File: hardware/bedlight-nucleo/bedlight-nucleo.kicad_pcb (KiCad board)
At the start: 2 copper layers, 76 x 76 mm, 10 parts, among them SW1 SW_Push, SW2 SW_Push, SW3 SW_Push, SW4 SW_Push, U1 Nucleo-32, U2 ULN2003A

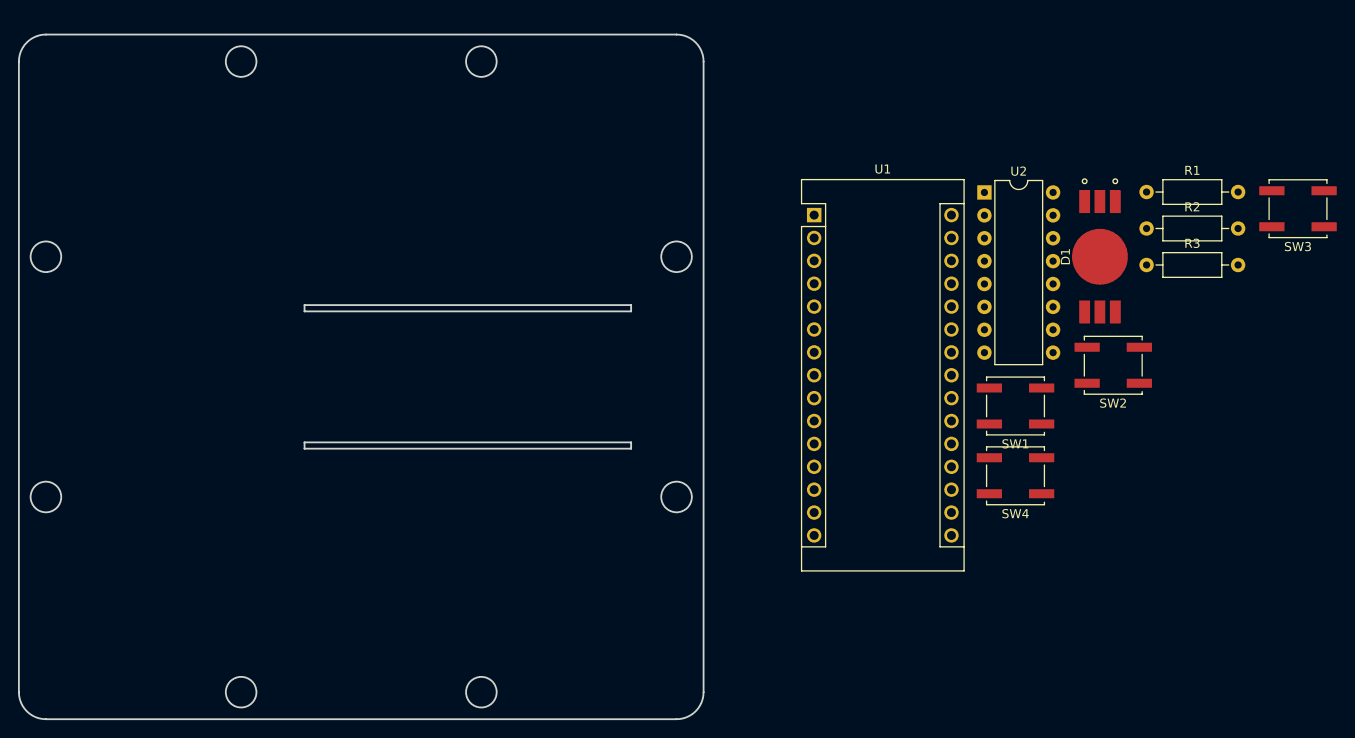
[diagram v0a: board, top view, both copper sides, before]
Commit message: Footprints partially placed
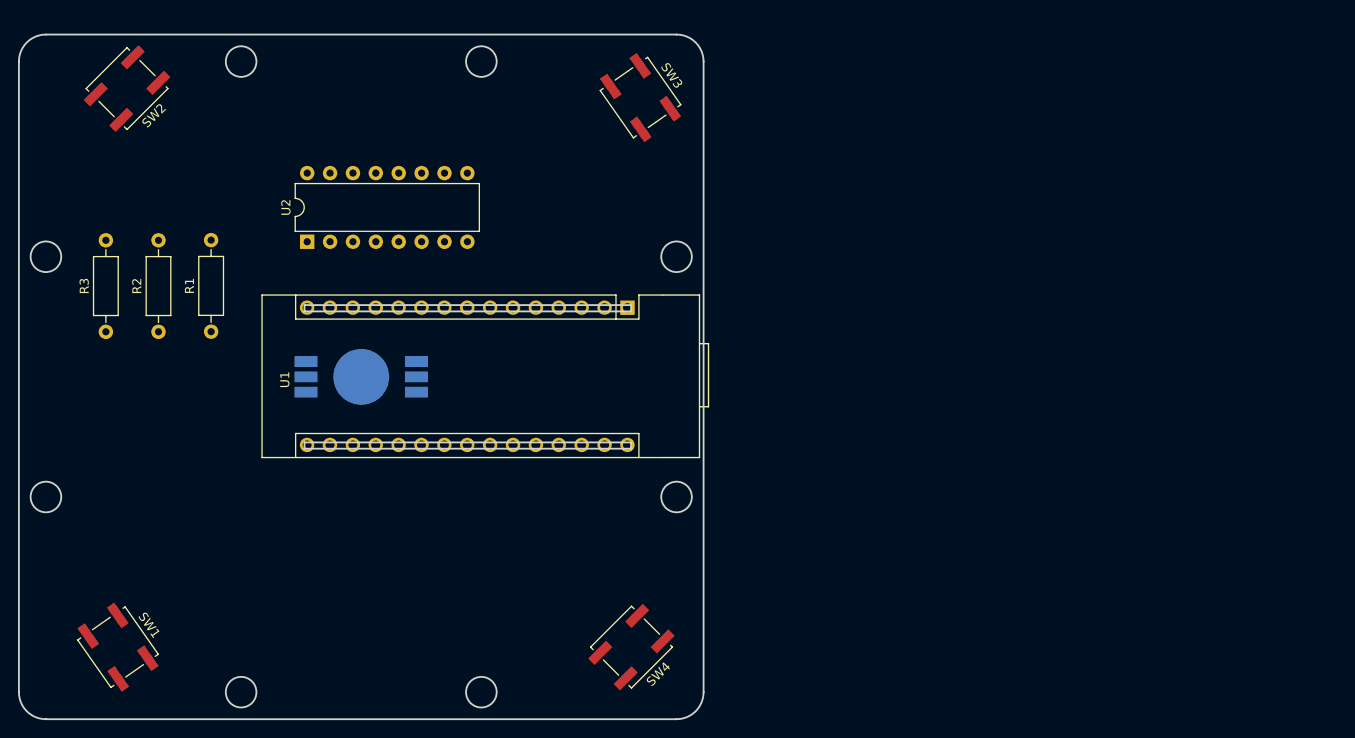
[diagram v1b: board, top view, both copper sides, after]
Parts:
- D1: moved to B.Cu
- U1: footprint Module:Arduino_Nano -> bedlight-nucleo:Nucleo-32
- moved R3 115.8 mm to (135.7, 107.3), turned to 90 degrees
- moved SW2 113.7 mm to (138.0, 80.3), turned to 45 degrees
- moved R2 110.3 mm to (141.5, 107.3), turned to 90 degrees
- moved R1 105.0 mm to (147.3, 107.3), turned to 90 degrees
- moved SW1 103.2 mm to (137.0, 142.3), turned to 125 degrees
- moved D1 83.1 mm to (164.0, 112.3), turned to 90 degrees
- moved U2 75.4 mm to (158.0, 97.3), turned to 90 degrees
- moved SW3 74.0 mm to (195.0, 81.3), turned to 125 degrees
- moved SW4 46.7 mm to (194.0, 142.3), turned to 45 degrees
- moved U1 23.1 mm to (193.5, 104.6), turned to 270 degrees
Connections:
- U1 pad 10: Net-(U1-Pad10) -> /OUT3
- U1 pad 11: Net-(U1-Pad11) -> /OUT2
- U1 pad 12: Net-(U1-Pad12) -> /OUT1
- U1 pad 13: Net-(U1-Pad13) -> /LED_RED
- U1 pad 14: /LED_RED -> /LED_GREEN
- U1 pad 15: /LED_GREEN -> /LED_BLUE
- U1 pad 16: /LED_BLUE -> Net-(U1-Pad16)
- U1 pad 9: Net-(U1-Pad9) -> /OUT4
- U2 pad 4: Net-(U2-Pad4) -> /OUT1
- U2 pad 5: Net-(U2-Pad5) -> /OUT2
- U2 pad 6: Net-(U2-Pad6) -> /OUT3
- U2 pad 7: Net-(U2-Pad7) -> /OUT4

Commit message: Routed
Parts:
- moved R3 10.9 mm to (146.5, 107.4)
- moved R1 10.2 mm to (137.1, 107.3)
- moved SW2 6.00 mm to (132.0, 80.3)
- moved SW1 5.39 mm to (132.0, 144.3), turned to 135 degrees
- moved SW4 2.83 mm to (196.0, 144.3)
- moved SW3 1.41 mm to (196.0, 80.3), turned to 135 degrees
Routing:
- net GND: track 0.00 -> 246.2 mm
- net /BUTTON2: track 0.00 -> 94.7 mm, vias 0 -> 1
- net /BUTTON1: track 0.00 -> 68.6 mm
- net +5V: track 0.00 -> 56.5 mm
- net /BUTTON3: track 0.00 -> 52.7 mm
- net /BUTTON4: track 0.00 -> 35.5 mm
- net Net-(R1-Pad2): track 0.00 -> 26.9 mm
- net Net-(D1-Pad1): track 0.00 -> 26.1 mm
- net Net-(R2-Pad2): track 0.00 -> 23.9 mm
- net Net-(R3-Pad2): track 0.00 -> 22.3 mm
- net Net-(D1-Pad2): track 0.00 -> 18.5 mm
- net Net-(D1-Pad3): track 0.00 -> 12.7 mm
- net /LED_BLUE: track 0.00 -> 7.42 mm
- net /OUT4: track 0.00 -> 7.32 mm
- net /OUT3: track 0.00 -> 7.32 mm
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- added copper zone on F.Cu, net GND
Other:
- outline, holes or cut-outs redrawn

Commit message: Added mounting holes
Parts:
- added H1: MountingHole, MountingHole:MountingHole_3.2mm_M3_DIN965_Pad, F.Cu at (177.3, 77.3)
- added H2: MountingHole, MountingHole:MountingHole_3.2mm_M3_DIN965_Pad, F.Cu at (129.0, 99.0)
- added H3: MountingHole, MountingHole:MountingHole_3.2mm_M3_DIN965_Pad, F.Cu at (150.7, 77.3)
- added H4: MountingHole, MountingHole:MountingHole_3.2mm_M3_DIN965_Pad, F.Cu at (129.0, 125.7)
- added H5: MountingHole, MountingHole:MountingHole_3.2mm_M3_DIN965_Pad, F.Cu at (199.0, 125.7)
- added H6: MountingHole, MountingHole:MountingHole_3.2mm_M3_DIN965_Pad, F.Cu at (150.7, 147.3)
- added H7: MountingHole, MountingHole:MountingHole_3.2mm_M3_DIN965_Pad, F.Cu at (199.0, 99.0)
- added H8: MountingHole, MountingHole:MountingHole_3.2mm_M3_DIN965_Pad, F.Cu at (177.3, 147.3)
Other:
- outline, holes or cut-outs redrawn
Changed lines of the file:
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@@
   (general
     (thickness 1.6)
-    (drawings 18)
+    (drawings 10)
     (tracks 112)
     (zones 0)
-    (modules 10)
+    (modules 18)
     (nets 41)
   )
@@
     (43 Eco2.User user)
     (44 Edge.Cuts user)
-    (45 Margin user)
-    (46 B.CrtYd user)
-    (47 F.CrtYd user)
+    (45 Margin user hide)
+    (46 B.CrtYd user hide)
+    (47 F.CrtYd user hide)
     (48 B.Fab user)
-    (49 F.Fab user)
+    (49 F.Fab user hide)
   )
   (setup
@@
     (mod_text_size 1 1)
     (mod_text_width 0.15)
-    (pad_size 1.524 1.524)
-    (pad_drill 0.762)
+    (pad_size 5.6 5.6)
+    (pad_drill 3.2)
     (pad_to_mask_clearance 0.05)
     (aux_axis_origin 0 0)
@@
     (add_net "Net-(U2-Pad9)")
   )
+  (module MountingHole:MountingHole_3.2mm_M3_DIN965_Pad (layer F.Cu)
+    (at 177.333333 147.333334)
+    (descr "Mounting Hole 3.2mm, M3, DIN965")
+    (tags "mounting hole 3.2mm m3 din965")
+    (attr virtual)
+    (fp_text reference H8 (at 0 -3.8) (layer F.SilkS)
+      (effects (font (size 1 1) (thickness 0.15)))
+    )
+    (fp_text value MountingHole (at 0 3.8) (layer F.Fab)
+      (effects (font (size 1 1) (thickness 0.15)))
+    )
+    (fp_text user %R (at 0.3 0) (layer F.Fab)
+      (effects (font (size 1 1) (thickness 0.15)))
+    )
+    (fp_circle (center 0 0) (end 2.8 0) (layer Cmts.User) (width 0.15))
+    (fp_circle (center 0 0) (end 3.05 0) (layer F.CrtYd) (width 0.05))
+    (pad 1 thru_hole circle (at 0 0) (size 5.6 5.6) (drill 3.2) (layers *.Cu *.Mask))
+  )
+  (module MountingHole:MountingHole_3.2mm_M3_DIN965_Pad (layer F.Cu)
+    (at 199 99)
+    (descr "Mounting Hole 3.2mm, M3, DIN965")
+    (tags "mounting hole 3.2mm m3 din965")
+    (attr virtual)
+    (fp_text reference H7 (at 0 -3.8) (layer F.SilkS)
+      (effects (font (size 1 1) (thickness 0.15)))
+    )
+    (fp_text value MountingHole (at 0 3.8) (layer F.Fab)
+      (effects (font (size 1 1) (thickness 0.15)))
+    )
+    (fp_text user %R (at 0.3 0) (layer F.Fab)
+      (effects (font (size 1 1) (thickness 0.15)))
+    )
+    (fp_circle (center 0 0) (end 2.8 0) (layer Cmts.User) (width 0.15))
+    (fp_circle (center 0 0) (end 3.05 0) (layer F.CrtYd) (width 0.05))
+    (pad 1 thru_hole circle (at 0 0) (size 5.6 5.6) (drill 3.2) (layers *.Cu *.Mask))
+  )
+  (module MountingHole:MountingHole_3.2mm_M3_DIN965_Pad (layer F.Cu)
+    (at 150.666666 147.333334)
+    (descr "Mounting Hole 3.2mm, M3, DIN965")
+    (tags "mounting hole 3.2mm m3 din965")
+    (attr virtual)
+    (fp_text reference H6 (at 0 -3.8) (layer F.SilkS)
+      (effects (font (size 1 1) (thickness 0.15)))
+    )
+    (fp_text value MountingHole (at 0 3.8) (layer F.Fab)
+      (effects (font (size 1 1) (thickness 0.15)))
+    )
+    (fp_text user %R (at 0.3 0) (layer F.Fab)
+      (effects (font (size 1 1) (thickness 0.15)))
+    )
+    (fp_circle (center 0 0) (end 2.8 0) (layer Cmts.User) (width 0.15))
+    (fp_circle (center 0 0) (end 3.05 0) (layer F.CrtYd) (width 0.05))
+    (pad 1 thru_hole circle (at 0 0) (size 5.6 5.6) (drill 3.2) (layers *.Cu *.Mask))
+  )
+  (module MountingHole:MountingHole_3.2mm_M3_DIN965_Pad (layer F.Cu)
+    (at 199 125.666667)
+    (descr "Mounting Hole 3.2mm, M3, DIN965")
+    (tags "mounting hole 3.2mm m3 din965")
+    (attr virtual)
+    (fp_text reference H5 (at 0 -3.8) (layer F.SilkS)
+      (effects (font (size 1 1) (thickness 0.15)))
+    )
+    (fp_text value MountingHole (at 0 3.8) (layer F.Fab)
+      (effects (font (size 1 1) (thickness 0.15)))
+    )
+    (fp_text user %R (at 0.3 0) (layer F.Fab)
+      (effects (font (size 1 1) (thickness 0.15)))
+    )
+    (fp_circle (center 0 0) (end 2.8 0) (layer Cmts.User) (width 0.15))
+    (fp_circle (center 0 0) (end 3.05 0) (layer F.CrtYd) (width 0.05))
+    (pad 1 thru_hole circle (at 0 0) (size 5.6 5.6) (drill 3.2) (layers *.Cu *.Mask))
+  )
+  (module MountingHole:MountingHole_3.2mm_M3_DIN965_Pad (layer F.Cu)
+    (at 129 125.666667)
+    (descr "Mounting Hole 3.2mm, M3, DIN965")
+    (tags "mounting hole 3.2mm m3 din965")
+    (attr virtual)
+    (fp_text reference H4 (at 0 -3.8) (layer F.SilkS)
+      (effects (font (size 1 1) (thickness 0.15)))
+    )
+    (fp_text value MountingHole (at 0 3.8) (layer F.Fab)
+      (effects (font (size 1 1) (thickness 0.15)))
+    )
+    (fp_text user %R (at 0.3 0) (layer F.Fab)
+      (effects (font (size 1 1) (thickness 0.15)))
+    )
+    (fp_circle (center 0 0) (end 2.8 0) (layer Cmts.User) (width 0.15))
+    (fp_circle (center 0 0) (end 3.05 0) (layer F.CrtYd) (width 0.05))
+    (pad 1 thru_hole circle (at 0 0) (size 5.6 5.6) (drill 3.2) (layers *.Cu *.Mask))
+  )
+  (module MountingHole:MountingHole_3.2mm_M3_DIN965_Pad (layer F.Cu)
+    (at 150.666666 77.333334)
+    (descr "Mounting Hole 3.2mm, M3, DIN965")
+    (tags "mounting hole 3.2mm m3 din965")
+    (attr virtual)
+    (fp_text reference H3 (at 0 -3.8) (layer F.SilkS)
+      (effects (font (size 1 1) (thickness 0.15)))
+    )
+    (fp_text value MountingHole (at 0 3.8) (layer F.Fab)
+      (effects (font (size 1 1) (thickness 0.15)))
+    )
+    (fp_text user %R (at 0.3 0) (layer F.Fab)
+      (effects (font (size 1 1) (thickness 0.15)))
+    )
+    (fp_circle (center 0 0) (end 2.8 0) (layer Cmts.User) (width 0.15))
+    (fp_circle (center 0 0) (end 3.05 0) (layer F.CrtYd) (width 0.05))
+    (pad 1 thru_hole circle (at 0 0) (size 5.6 5.6) (drill 3.2) (layers *.Cu *.Mask))
+  )
+  (module MountingHole:MountingHole_3.2mm_M3_DIN965_Pad (layer F.Cu)
+    (at 129 99)
+    (descr "Mounting Hole 3.2mm, M3, DIN965")
+    (tags "mounting hole 3.2mm m3 din965")
+    (attr virtual)
+    (fp_text reference H2 (at 0 -3.8) (layer F.SilkS)
+      (effects (font (size 1 1) (thickness 0.15)))
+    )
+    (fp_text value MountingHole (at 0 3.8) (layer F.Fab)
+      (effects (font (size 1 1) (thickness 0.15)))
+    )
+    (fp_text user %R (at 0.3 0) (layer F.Fab)
+      (effects (font (size 1 1) (thickness 0.15)))
+    )
+    (fp_circle (center 0 0) (end 2.8 0) (layer Cmts.User) (width 0.15))
+    (fp_circle (center 0 0) (end 3.05 0) (layer F.CrtYd) (width 0.05))
+    (pad 1 thru_hole circle (at 0 0) (size 5.6 5.6) (drill 3.2) (layers *.Cu *.Mask))
+  )
+  (module MountingHole:MountingHole_3.2mm_M3_DIN965_Pad (layer F.Cu)
+    (at 177.333333 77.333334)
+    (descr "Mounting Hole 3.2mm, M3, DIN965")
+    (tags "mounting hole 3.2mm m3 din965")
+    (attr virtual)
+    (fp_text reference H1 (at 0 -3.8) (layer F.SilkS)
+      (effects (font (size 1 1) (thickness 0.15)))
+    )
+    (fp_text value MountingHole (at 0 3.8) (layer F.Fab)
+      (effects (font (size 1 1) (thickness 0.15)))
+    )
+    (fp_text user %R (at 0.3 0) (layer F.Fab)
+      (effects (font (size 1 1) (thickness 0.15)))
+    )
+    (fp_circle (center 0 0) (end 2.8 0) (layer Cmts.User) (width 0.15))
+    (fp_circle (center 0 0) (end 3.05 0) (layer F.CrtYd) (width 0.05))
+    (pad 1 thru_hole circle (at 0 0) (size 5.6 5.6) (drill 3.2) (layers *.Cu *.Mask))
+  )
   (module bedlight-nucleo:Nucleo-32 (layer F.Cu)
     (at 193.548 104.648 270)
@@
   (gr_line (start 164 111.333334) (end 164 113.333334) (layer Dwgs.User) (width 0.15))
   (gr_arc (start 129 147.333334) (end 126 147.333334) (angle -90) (layer Edge.Cuts) (width 0.2))
-  (gr_circle (center 129 125.666667) (end 130.7 125.666667) (layer Edge.Cuts) (width 0.2))
-  (gr_circle (center 150.666666 77.333334) (end 152.366666 77.333334) (layer Edge.Cuts) (width 0.2))
   (gr_arc (start 199 147.333334) (end 199 150.333334) (angle -90) (layer Edge.Cuts) (width 0.2))
   (gr_arc (start 129 77.333334) (end 129 74.333334) (angle -90) (layer Edge.Cuts) (width 0.2))
   (gr_line (start 129 74.333334) (end 199 74.333334) (layer Edge.Cuts) (width 0.2))
   (gr_line (start 199 150.333334) (end 129 150.333334) (layer Edge.Cuts) (width 0.2))
-  (gr_circle (center 129 99) (end 130.7 99) (layer Edge.Cuts) (width 0.2))
-  (gr_circle (center 177.333333 77.333334) (end 179.033333 77.333334) (layer Edge.Cuts) (width 0.2))
   (gr_line (start 126 147.333334) (end 126 77.333334) (layer Edge.Cuts) (width 0.2))
   (gr_line (start 202 77.333334) (end 202 147.333334) (layer Edge.Cuts) (width 0.2))
-  (gr_circle (center 150.666666 147.333334) (end 152.366666 147.333334) (layer Edge.Cuts) (width 0.2))
-  (gr_circle (center 177.333333 147.333334) (end 179.033333 147.333334) (layer Edge.Cuts) (width 0.2))
-  (gr_circle (center 199 125.666667) (end 200.7 125.666667) (layer Edge.Cuts) (width 0.2))
   (gr_arc (start 199 77.333334) (end 202 77.333334) (angle -90) (layer Edge.Cuts) (width 0.2))
-  (gr_circle (center 199 99) (end 200.7 99) (layer Edge.Cuts) (width 0.2))
   (segment (start 149.727 110.633334) (end 146.526 107.432334) (width 0.508) (layer B.Cu) (net 1))
   (segment (start 157.875 110.633334) (end 149.727 110.633334) (width 0.508) (layer B.Cu) (net 1))

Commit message: Planes remake
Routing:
- added copper zone on B.Cu, net (none)
- added copper zone on F.Cu, net (none)
- removed copper zone on F.Cu, net GND
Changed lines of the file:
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@@
   (segment (start 173.228 103.822063) (end 173.24 103.810063) (width 0.508) (layer F.Cu) (net 40))
   (segment (start 173.228 104.648) (end 173.228 103.822063) (width 0.508) (layer F.Cu) (net 40))
-  (zone (net 8) (net_name GND) (layer F.Cu) (hatch edge 0.508)
+  (zone (net 0) (net_name "") (layer B.Cu) (hatch edge 0.508)
     (connect_pads (clearance 0.508))
     (min_thickness 0.254)
@@
     (polygon
       (pts
-        (xy 200.406 137.922) (xy 127.254 137.922) (xy 127.254 85.344) (xy 200.406 85.344)
+        (xy 200 148) (xy 128 148) (xy 128 77) (xy 200 77)
       )
     )
+  )
+  (zone (net 0) (net_name "") (layer F.Cu) (hatch edge 0.508)
+    (connect_pads (clearance 0.508))
+    (min_thickness 0.254)
+    (fill yes (arc_segments 32) (thermal_gap 0.508) (thermal_bridge_width 0.508))
+    (polygon
+      (pts
+        (xy 200 148) (xy 128 148) (xy 128 77) (xy 200 77)
+      )
+    )
